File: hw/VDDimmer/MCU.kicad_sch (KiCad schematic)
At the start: 22 parts, among them J1 USB-C 16P, J11 BTN1, J12 BTN2, J13 EXP 3V3/GND/SDA/SCL/EN/IO0, J14 UART1 3V3/GND/TX/RX, U1 ESP32-S3-WROOM-1U-N16

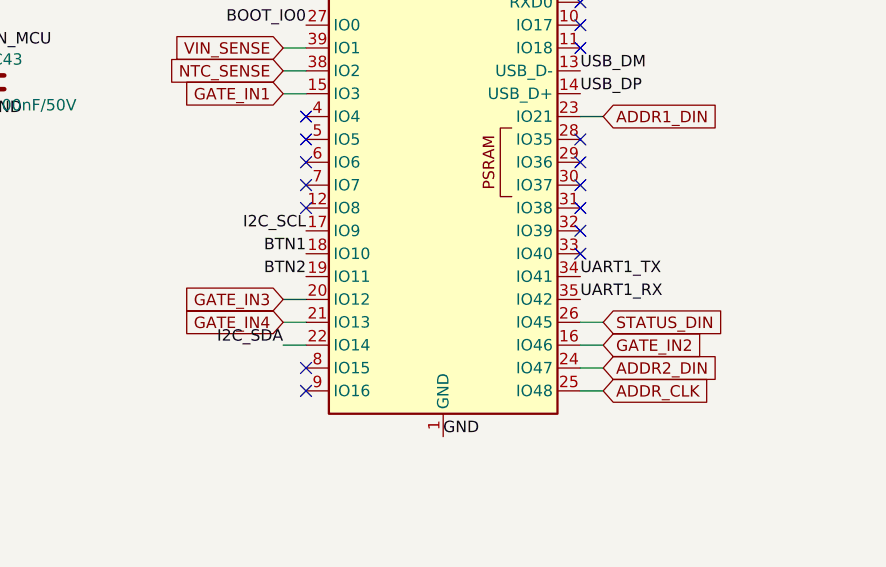
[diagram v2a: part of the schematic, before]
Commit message: Route MCU signals: I2C, UART, buttons, boot, enable, analogue sense
Second U1 reshuffle, driven by measured geometry rather than convenience.
J13's six pins sit at y = 95/97.54/100.08/102.62/105.16/107.70 with 0.84 mm
gaps between pads; U1's right column sits at 1.27 mm pitch with 0.9 mm pads.
The odd-numbered right-column pads line up with J13's gaps and the even ones
line up with J13's pins, so:
  p15 106.485 GATE_IN1 -> gap 106.43     p18 102.675 I2C_SCL -> pin 102.62
  p17 103.945 GATE_IN2 -> gap 103.89     p20 100.135 I2C_SDA -> pin 100.08
  p19 101.405 GATE_IN3 -> gap 101.35
  p21  98.865 GATE_IN4 -> gap  98.81
Both I2C lines are now single straight segments into their header pins, and
all four gate-driver inputs pass J13 without a jog.

BTN1/BTN2 moved to U1's top row (IO40/IO39) and UART1_TX/RX swapped (IO42/IO41)
so that all four westbound nets nest instead of interleaving. They now leave
U1 southward under the module and run west on four lanes at y =
96.6/97.2/97.9/105.0. J14 moved to (108,100) rot 90 so its pins face them;
R40 moved to (128,109) so EN_MCU's pull-up is on the EN lane instead of
across four of them.

NTC_SENSE and VIN_SENSE stay on IO2/IO1 -- the only ADC-capable pins on that
row -- and run east above U1 on lanes y = 89.5 and 86.0. RT1 and R29 rotated
180 so the divider's midpoint pads are adjacent (they were at opposite outer
ends, with GND and +3V3 between them).

Bottom-layer copper added: BOOT_IO0 3.5 mm and EN_MCU 5.3 mm. U1's right pad
column (x 148.6..150.1, y 92..107) and the GATE_IN1 lane together seal off the
bottom-right corner: the window between U1.15's pad and U1's bottom row is
0.565 mm, and a 0.25 mm trace needs 0.65 mm. Both hops are ~80 mm from the
buck and do not touch the 8.5.3 keepout.

DRC 0 errors, 0 phantom pads, unconnected 146 -> 130.

Co-Authored-By: Claude Opus 5 (1M context) <noreply@anthropic.com>
Claude-Session: https://claude.ai/code/session_01XeXr1isxVCg8kRo5Eh8BHM
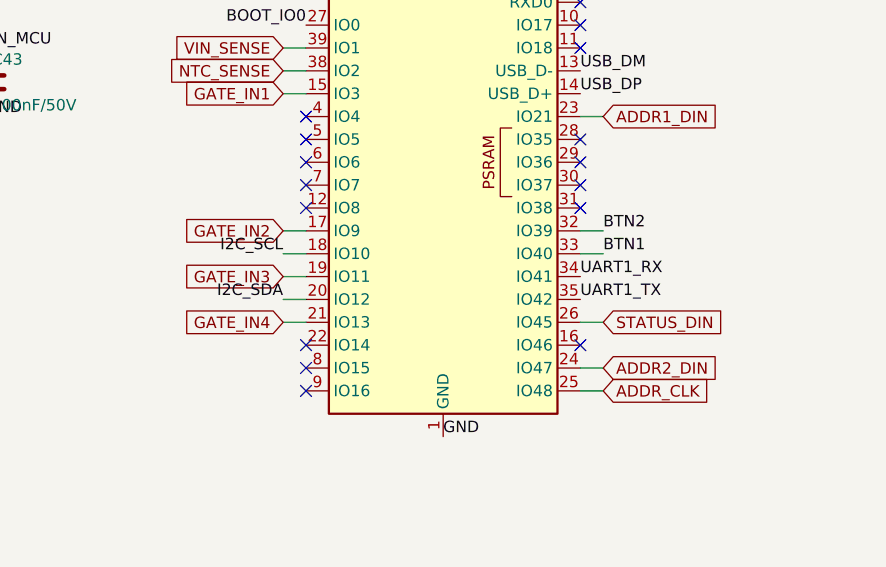
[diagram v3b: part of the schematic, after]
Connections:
- net BTN1: now also U1.33 (IO40); no longer U1.18 (IO10)
- net BTN2: now also U1.32 (IO39); no longer U1.19 (IO11)
- net GATE_IN2: now also U1.17 (IO9); no longer U1.16 (IO46)
- net GATE_IN3: now also U1.19 (IO11); no longer U1.20 (IO12)
- net I2C_SCL: now also U1.18 (IO10); no longer U1.17 (IO9)
- net I2C_SDA: now also U1.20 (IO12); no longer U1.22 (IO14)
- net UART1_RX: now also U1.34 (IO41); no longer U1.35 (IO42)
- net UART1_TX: now also U1.35 (IO42); no longer U1.34 (IO41)
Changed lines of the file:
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@@
-	)
-	(no_connect
-		(at 214.63 124.46)
-	)
-	(no_connect
-		(at 214.63 127)
 	)
 	(no_connect
@@
 	(no_connect
 		(at 184.15 121.92)
+	)
+	(no_connect
+		(at 184.15 137.16)
+	)
+	(no_connect
+		(at 214.63 137.16)
 	)
 	(wire
@@
 	(wire
 		(pts
-			(xy 214.63 137.16)
-			(xy 217.17 137.16)
+			(xy 184.15 134.62)
+			(xy 181.61 134.62)
+		)
+	)
+	(wire
+		(pts
+			(xy 214.63 111.76)
+			(xy 217.17 111.76)
+		)
+	)
+	(wire
+		(pts
+			(xy 214.63 139.7)
+			(xy 217.17 139.7)
+		)
+	)
+	(wire
+		(pts
+			(xy 214.63 134.62)
+			(xy 217.17 134.62)
+		)
+	)
+	(wire
+		(pts
+			(xy 184.15 124.46)
+			(xy 181.61 124.46)
+		)
+	)
+	(wire
+		(pts
+			(xy 184.15 127)
+			(xy 181.61 127)
+		)
+	)
+	(wire
+		(pts
+			(xy 184.15 129.54)
+			(xy 181.61 129.54)
 		)
 	)
@@
 	(wire
 		(pts
-			(xy 184.15 134.62)
-			(xy 181.61 134.62)
-		)
-	)
-	(wire
-		(pts
-			(xy 184.15 137.16)
-			(xy 181.61 137.16)
-		)
-	)
-	(wire
-		(pts
-			(xy 214.63 111.76)
-			(xy 217.17 111.76)
-		)
-	)
-	(wire
-		(pts
-			(xy 214.63 139.7)
-			(xy 217.17 139.7)
-		)
-	)
-	(wire
-		(pts
-			(xy 214.63 134.62)
-			(xy 217.17 134.62)
+			(xy 214.63 124.46)
+			(xy 217.17 124.46)
+		)
+	)
+	(wire
+		(pts
+			(xy 214.63 127)
+			(xy 217.17 127)
 		)
 	)
@@
 	)
 	(label "BTN1"
-		(at 184.15 127 180)
-		(effects
-			(font
-				(size 1.27 1.27)
-			)
-			(justify right bottom)
-		)
-	)
-	(label "BTN1"
 		(at 299.72 63.5 0)
 		(effects
@@
 	)
 	(label "BTN2"
-		(at 184.15 129.54 180)
-		(effects
-			(font
-				(size 1.27 1.27)
-			)
-			(justify right bottom)
-		)
-	)
-	(label "BTN2"
 		(at 317.5 63.5 0)
 		(effects
@@
 	)
 	(label "I2C_SCL"
-		(at 184.15 124.46 180)
-		(effects
-			(font
-				(size 1.27 1.27)
-			)
-			(justify right bottom)
-		)
-	)
-	(label "I2C_SCL"
 		(at 294.64 113.03 180)
 		(effects
@@
 	)
 	(label "UART1_TX"
-		(at 214.63 129.54 0)
-		(effects
-			(font
-				(size 1.27 1.27)
-			)
-			(justify left bottom)
-		)
-	)
-	(label "UART1_TX"
 		(at 294.64 162.56 180)
 		(effects
@@
 			)
 			(justify right bottom)
-		)
-	)
-	(label "UART1_RX"
-		(at 214.63 132.08 0)
-		(effects
-			(font
-				(size 1.27 1.27)
-			)
-			(justify left bottom)
 		)
 	)
@@
 		)
 	)
+	(label "I2C_SCL"
+		(at 181.61 127 180)
+		(effects
+			(font
+				(size 1.27 1.27)
+			)
+			(justify right bottom)
+		)
+	)
 	(label "I2C_SDA"
-		(at 181.61 137.16 180)
-		(effects
-			(font
-				(size 1.27 1.27)
-			)
-			(justify right bottom)
+		(at 181.61 132.08 180)
+		(effects
+			(font
+				(size 1.27 1.27)
+			)
+			(justify right bottom)
+		)
+	)
+	(label "BTN2"
+		(at 217.17 124.46 0)
+		(effects
+			(font
+				(size 1.27 1.27)
+			)
+			(justify left bottom)
+		)
+	)
+	(label "BTN1"
+		(at 217.17 127 0)
+		(effects
+			(font
+				(size 1.27 1.27)
+			)
+			(justify left bottom)
+		)
+	)
+	(label "UART1_RX"
+		(at 214.63 129.54 0)
+		(effects
+			(font
+				(size 1.27 1.27)
+			)
+			(justify left bottom)
+		)
+	)
+	(label "UART1_TX"
+		(at 214.63 132.08 0)
+		(effects
+			(font
+				(size 1.27 1.27)
+			)
+			(justify left bottom)
 		)
 	)
@@
 		)
 	)
+	(global_label "GATE_IN4"
+		(shape input)
+		(at 181.61 134.62 180)
+		(effects
+			(font
+				(size 1.27 1.27)
+			)
+			(justify right)
+		)
+	)
+	(global_label "ADDR1_DIN"
+		(shape input)
+		(at 217.17 111.76 0)
+		(effects
+			(font
+				(size 1.27 1.27)
+			)
+			(justify left)
+		)
+	)
+	(global_label "ADDR2_DIN"
+		(shape input)
+		(at 217.17 139.7 0)
+		(effects
+			(font
+				(size 1.27 1.27)
+			)
+			(justify left)
+		)
+	)
+	(global_label "STATUS_DIN"
+		(shape input)
+		(at 217.17 134.62 0)
+		(effects
+			(font
+				(size 1.27 1.27)
+			)
+			(justify left)
+		)
+	)
+	(global_label "ADDR_CLK"
+		(shape input)
+		(at 217.17 142.24 0)
+		(effects
+			(font
+				(size 1.27 1.27)
+			)
+			(justify left)
+		)
+	)
 	(global_label "GATE_IN2"
 		(shape input)
-		(at 217.17 137.16 0)
-		(effects
-			(font
-				(size 1.27 1.27)
-			)
-			(justify left)
+		(at 181.61 124.46 180)
+		(effects
+			(font
+				(size 1.27 1.27)
+			)
+			(justify right)
 		)
 	)
 	(global_label "GATE_IN3"
 		(shape input)
-		(at 181.61 132.08 180)
+		(at 181.61 129.54 180)
 		(effects
 			(font
@@
 		)
 	)
-	(global_label "GATE_IN4"
-		(shape input)
-		(at 181.61 134.62 180)
-		(effects
-			(font
-				(size 1.27 1.27)
-			)
-			(justify right)
-		)
-	)
-	(global_label "ADDR1_DIN"
-		(shape input)
-		(at 217.17 111.76 0)
-		(effects
-			(font
-				(size 1.27 1.27)
-			)
-			(justify left)
-		)
-	)
-	(global_label "ADDR2_DIN"
-		(shape input)
-		(at 217.17 139.7 0)
-		(effects
-			(font
-				(size 1.27 1.27)
-			)
-			(justify left)
-		)
-	)
-	(global_label "STATUS_DIN"
-		(shape input)
-		(at 217.17 134.62 0)
-		(effects
-			(font
-				(size 1.27 1.27)
-			)
-			(justify left)
-		)
-	)
-	(global_label "ADDR_CLK"
-		(shape input)
-		(at 217.17 142.24 0)
-		(effects
-			(font
-				(size 1.27 1.27)
-			)
-			(justify left)
-		)
-	)

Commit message: Schematic pass: MPN/LCSC/Manufacturer on all 79 sourced parts
F1 -> "8A 250V", U3 -> "BL1117-33CX", J2 -> "VIN 12V" (was "VIN 9-24V",
which invited 24 V into an 18 V TVS). R11/R12 values cleaned to "47R" with
the DNP intent moved into the Assembly field. ERC still 0 violations.

Every sourced part now carries MPN, LCSC and Manufacturer, plus an Assembly
note anywhere the choice needs explaining - why D5 is an SMBJ18A, why R30's
current rating still needs checking, why L1 is candidate-only.

Two things this pass could NOT do, both because no MCP tool writes them:

- KiCad's (dnp yes) attribute. R11 and R12 must be flagged in the GUI; their
  Assembly fields say so. All five text-only DNPs were in this state, but
  L3/C20/R31 are now fitted by decision, so only R11/R12 remain.
- Fields on units 2-5 of a multi-unit symbol. Konnect writes unit 1 only,
  where the GUI propagates to all units. U4/U5 are 5-unit 74HCT125s, so
  grouping a BOM by MPN splits U5 into two lines and would order 3 of a
  2-off part. tools/export-bom.sh groups by Value+Footprint instead, which
  collapses correctly - 49 lines, 96 parts, and the 15 lines without an LCSC
  are exactly the mounting holes and hand-fit connectors.

Also checked and left alone: the U4/U5 symbol's lib_id is 74AHCT125 while its
value is 74HCT125. AHCT would be the conventional WS2812 level shifter, but
JLC has 70 of it in SO-14 against 88,003 of the HCT part, and HCT is fine here
- TTL inputs, 15 ns against 300 ns bit times. The value is the buyable intent.

Co-Authored-By: Claude Opus 5 (1M context) <noreply@anthropic.com>
Claude-Session: https://claude.ai/code/session_01QsYnM2qRBWQsyKPH1v7rLR
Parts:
- C40, C44: LCSC (none) -> C15850; MPN (none) -> CL21A106KAYNNNE; Manufacturer (none) -> Samsung Electro-Mechanics
- C41, C42, C43: LCSC (none) -> C14663; MPN (none) -> CC0603KRX7R9BB104; Manufacturer (none) -> YAGEO
- D8: Assembly (none) -> UMW second source; genuine ST is C7519 if preferred; LCSC (none) -> C2687116; MPN (none) -> USBLC6-2SC6; Manufacturer (none) -> UMW
- D9: LCSC (none) -> C8678; MPN (none) -> SS34; Manufacturer (none) -> MDD
- R40, R43, R44: LCSC (none) -> C17414; MPN (none) -> 0805W8F1002T5E; Manufacturer (none) -> UNI-ROYAL
- R41, R42: LCSC (none) -> C27834; MPN (none) -> 0805W8F5101T5E; Manufacturer (none) -> UNI-ROYAL
- U1: Assembly (none) -> 355 mA TX / 95 mA RX - this is the load U3 must carry; LCSC (none) -> C2980298; MPN (none) -> ESP32-S3-WROOM-1U-N16; Manufacturer (none) -> Espressif Systems

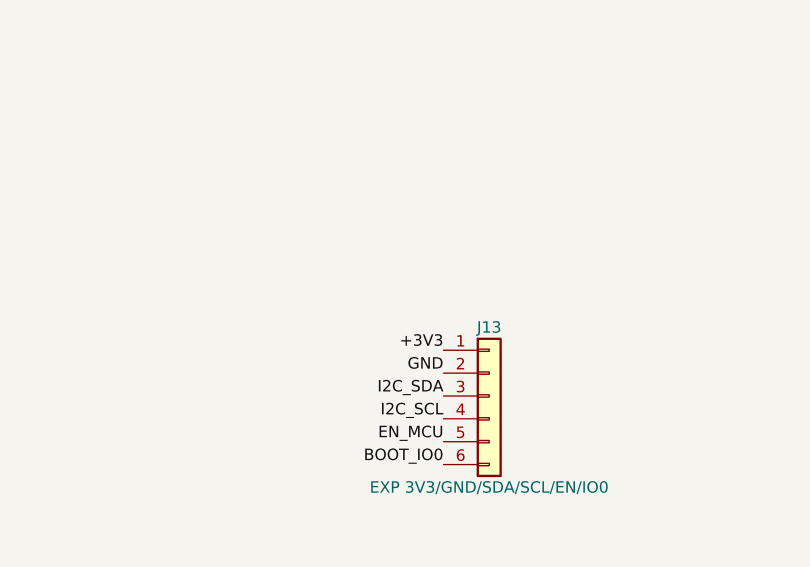
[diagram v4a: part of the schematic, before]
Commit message: Fix six drill defects, fit the I2C pull-ups, add the board ID
Drill defects
-------------
hole_to_hole and holes_co_located are downgraded to warning in .kicad_pro, so
the board reported "DRC 0 errors" while carrying five hole_to_hole and one
holes_co_located -- two of them with physically overlapping drills. Same shape
of trap as the split-net lesson already in HANDOFF.

Five vias deleted, each proven non-load-bearing first by checking which track
endpoints actually land on it. In every overlapping pair only one via carried a
track; the other was a bare stitching via with its twin 0.1-0.5 mm away.
d85c5d26 was redundant by construction -- 1 mm from J2's PTH GND pad, which
already ties both layers. afb88017 was an exact duplicate of a14092cd.
Afterwards GND is still one connected group, the split-net count is unchanged
at 12, and via count went 192 -> 187.

I2C pull-ups (R45, R46)
-----------------------
4.7k 0805, C17673, per the 2026-08-29 decision. Verified against the exported
netlist rather than the tools' return values, because the pins are tied with a
plain +3V3 net label -- the convention J13's own supply pin uses on this sheet.
Had that not merged with the power net the pull-ups would have pulled to
nothing, which is the silent failure the decision existed to prevent.

  +3V3          15 nodes  ... J13.1 R43.1 R44.1 R45.1 R46.1 U1.2 U3.2
  /MCU/I2C_SDA   3 nodes  J13.3  R45.2  U1.20
  /MCU/I2C_SCL   3 nodes  J13.4  R46.2  U1.18

The taps run on B.Cu because ADDR1_DIN crosses the whole board on F.Cu at
y=96.33, x 149.35-168.60, walling +3V3 (which reaches J13.1 at y=95) off from
the I2C lines at y=100.14 and 102.67. There is no F.Cu-only path; going round
its east end costs ~30 mm and still needs via hops over the GATE_IN verticals.
B.Cu there is bare GND pour and J13's pads 1/3/4 are through-hole, so they are
reachable from below with no via at that end.

Both parts are rotated 180 deg. They arrive with pad 1 (+3V3) west, which would
force the SDA return to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
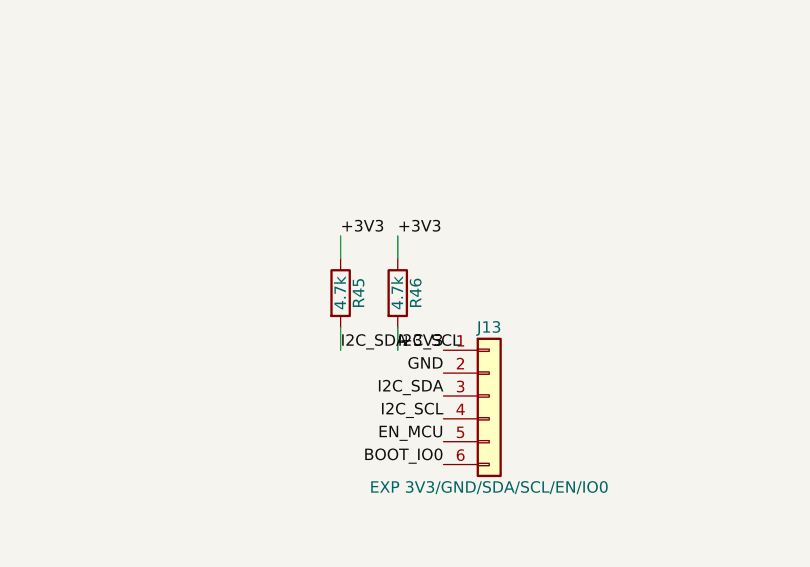
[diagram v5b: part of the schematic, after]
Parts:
- added R45, R46: 4.7k, Resistor_SMD:R_0805_2012Metric, symbol Device:R
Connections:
- net +3V3: now also R45.1, R46.1
- net I2C_SCL: now also R46.2
- net I2C_SDA: now also R45.2

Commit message: Source J1: it was never hand-fit by decision, just missing a part number
J1 is C165948, TYPE-C-31-M-12 from Korean Hroparts Elec -- 315,519 in stock at
$0.1853, and precisely the part the footprint is named for
(USB_C_Receptacle_HRO_TYPE-C-31-M-12; HRO = Korean Hroparts).

It had no LCSC code, and export-cpl.sh treats unsourced parts as hand-fit, so it
was classified out of the SMT assembly by accident rather than by choice. Every
prior note treated "J1 is hand-fit per spec 10" as a decision to argue with,
when the real cause was missing sourcing data.

The rule that actually separates the connectors is mounting type, not the spec:

  J1        SMD (surface mount, right angle)  -> machine-placed
  J2-J14    through-hole                      -> correctly hand-fit, because
            JLC's SMT service does not place THT parts

JLC stocks the others too (S2B-XH-A is C157931, 55k in stock), so the temptation
to "fix" them the same way is there. Recorded that it would be wrong.

  CPL      77 -> 78 machine-placed
  BOM      34 -> 35 lines
  cost     $10.450 -> $10.635 per board

Consequences carried forward:

  * Assembly edge clearance worsened. J1 sits on the west edge, so the closest
    machine-placed copper to it fell 4.55 -> 1.80 mm. There was already no pair
    of opposite edges clearing 5 mm, so JLC rails remain likely.
  * J1's rotation reaches the CPL as KiCad's 270 deg, uncorrected. USB-C
    receptacles are a classic case of a fab library using a different reference
    orientation -- check the placement preview before releasing.

ERC 0, DRC 0 errors, 165 warnings. Bundle cross-checks at 78/78 designators with
no orphans and every line carrying an LCSC code. Parity is 6 (the five swapped
caps plus J1's new fields); cosmetic, one F8 sync clears it.

Co-Authored-By: Claude Opus 5 (1M context) <noreply@anthropic.com>
Claude-Session: https://claude.ai/code/session_01AnYUdWpnpbT2cnPRPqtfVa
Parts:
- J1: Assembly (none) -> MACHINE-PLACED. SMD (surface mount, right angle) so it belo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; LCSC (none) -> C165948; MPN (none) -> TYPE-C-31-M-12; Manufacturer (none) -> Korean Hroparts Elec
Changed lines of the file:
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@@
 			)
 		)
-	)
+		(property "Assembly" "MACHINE-PLACED. SMD (surface mount, right angle) so it belongs in the SMT assembly, unlike J2-J14 which are through-hole and correctly hand-fit. 16 pads at 0.5 mm pitch plus four shell legs is not sensibly hand-soldered"
+			(at 44.45 175.26 0)
+			(hide yes)
+			(effects
+				(font
+					(size 1.27 1.27)
+				)
+			)
+		)
+		(property "LCSC" "C165948"
+			(at 44.45 175.26 0)
+			(hide yes)
+			(effects
+				(font
+					(size 1.27 1.27)
+				)
+			)
+		)
+		(property "MPN" "TYPE-C-31-M-12"
+			(at 44.45 175.26 0)
+			(hide yes)
+			(effects
+				(font
+					(size 1.27 1.27)
+				)
+			)
+		)
+		(property "Manufacturer" "Korean Hroparts Elec"
+			(at 44.45 175.26 0)
+			(hide yes)
+			(effects
+				(font
+					(size 1.27 1.27)
+				)
+			)
+		))
 	(symbol
 		(lib_id "Connector_Generic:Conn_01x02")

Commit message: Swap U1 to the on-board-antenna module
ESP32-S3-WROOM-1U-N16 (C2980298) -> ESP32-S3-WROOM-1-N16R8 (C2913202).

Only the footprint, value and part fields change. The lib_id was already
RF_Module:ESP32-S3-WROOM-1 -- KiCad uses one symbol for both variants because
they share a pad layout, the -1U being the same module with the antenna section
removed. So every net keeps its pin and no symbol swap is needed.

The N16R8 carries 8 MB of PSRAM the firmware does not use. There is no plain
-1-N16 at JLCPCB, and the PSRAM pins (IO35-37) do not collide with the design's
pin map, so this is deliberate. It also has 37918 in stock against 4246.

Verified by reading the file back rather than trusting the tool's return value:
no WROOM-1U string remains in MCU.kicad_sch.

Co-Authored-By: Claude Opus 5 (1M context) <noreply@anthropic.com>
Claude-Session: https://claude.ai/code/session_01YZHVU8aymL4RkLeCfwomwj
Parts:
- U1: value ESP32-S3-WROOM-1U-N16 -> ESP32-S3-WROOM-1-N16R8; footprint RF_Module:ESP32-S3-WROOM-1U -> RF_Module:ESP32-S3-WROOM-1; LCSC C2980298 -> C2913202; MPN ESP32-S3-WROOM-1U-N16 -> ESP32-S3-WROOM-1-N16R8
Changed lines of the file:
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@@
 			)
 		)
-		(property "Value" "ESP32-S3-WROOM-1U-N16"
+		(property "Value" "ESP32-S3-WROOM-1-N16R8"
 			(at 212.09 92.71 0)
 			(show_name no)
@@
 			)
 		)
-		(property "Footprint" "RF_Module:ESP32-S3-WROOM-1U"
+		(property "Footprint" "RF_Module:ESP32-S3-WROOM-1"
 			(at 199.39 119.38 0)
 			(hide yes)
@@
 			)
 		)
-		(property "LCSC" "C2980298"
+		(property "LCSC" "C2913202"
 			(at 199.39 119.38 0)
 			(hide yes)
@@
 			)
 		)
-		(property "MPN" "ESP32-S3-WROOM-1U-N16"
+		(property "MPN" "ESP32-S3-WROOM-1-N16R8"
 			(at 199.39 119.38 0)
 			(hide yes)
